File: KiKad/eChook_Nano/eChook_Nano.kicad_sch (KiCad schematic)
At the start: 52 parts, among them J1 Expansion, Q1 BC547, U1 Arduino_Nano_v3.x, U2 TSR_1-2450, U3 MCP6002-xP

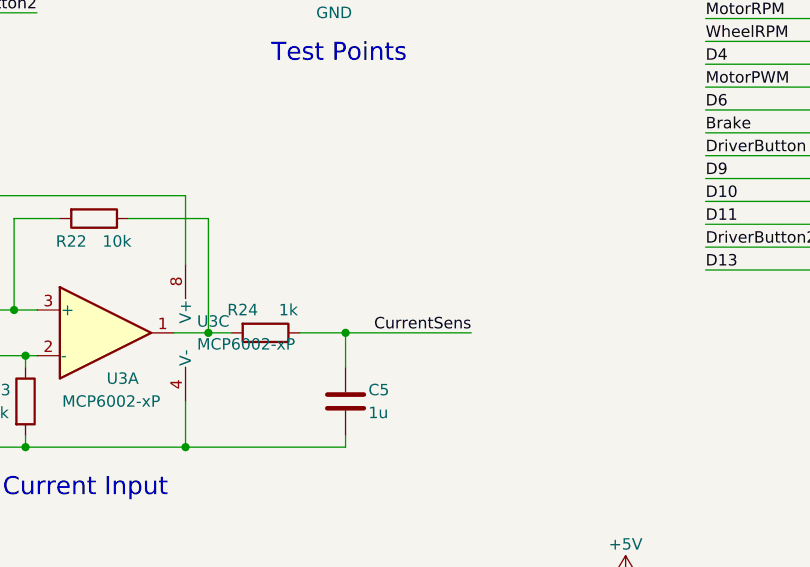
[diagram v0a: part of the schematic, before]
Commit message: Added 3D models and layout/silkscreen improvements
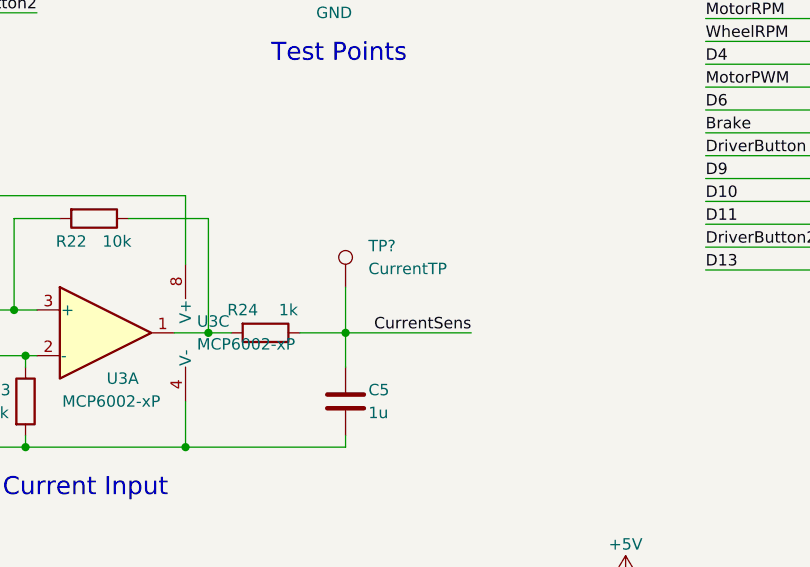
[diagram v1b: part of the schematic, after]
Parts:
- added TP?: CurrentTP, TestPoint:TestPoint_Pad_D3.0mm, symbol Connector:TestPoint
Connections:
- net CurrentSens: now also TP?.1
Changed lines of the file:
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@@
+    (stroke (width 0) (type default) (color 0 0 0 0))
+  )
+  (wire (pts (xy 93.98 124.46) (xy 93.98 129.54))
     (stroke (width 0) (type default) (color 0 0 0 0))
   )
@@
     )
     (property "Datasheet" "" (id 3) (at 34.29 187.325 0)
+      (effects (font (size 1.27 1.27)) hide)
+    )
+    (pin "1")
+  )
+  (symbol (lib_id "Connector:TestPoint") (at 93.98 124.46 0) (unit 1)
+    (in_bom yes) (on_board yes) (fields_autoplaced)
+    (property "Reference" "TP?" (id 0) (at 96.52 119.8879 0)
+      (effects (font (size 1.27 1.27)) (justify left))
+    )
+    (property "Value" "CurrentTP" (id 1) (at 96.52 122.4279 0)
+      (effects (font (size 1.27 1.27)) (justify left))
+    )
+    (property "Footprint" "TestPoint:TestPoint_Pad_D3.0mm" (id 2) (at 99.06 124.46 0)
+      (effects (font (size 1.27 1.27)) hide)
+    )
+    (property "Datasheet" "~" (id 3) (at 99.06 124.46 0)
       (effects (font (size 1.27 1.27)) hide)
     )
@@
       (reference "TP8") (unit 1) (value "ThrottleTP") (footprint "TestPoint:TestPoint_Pad_D3.0mm")
     )
+    (path "/dca3b52c-6cfb-46fe-8a89-560fb218906c"
+      (reference "TP?") (unit 1) (value "CurrentTP") (footprint "TestPoint:TestPoint_Pad_D3.0mm")
+    )
     (path "/ea7c53f9-3aa8-4198-9879-de95a5257915"

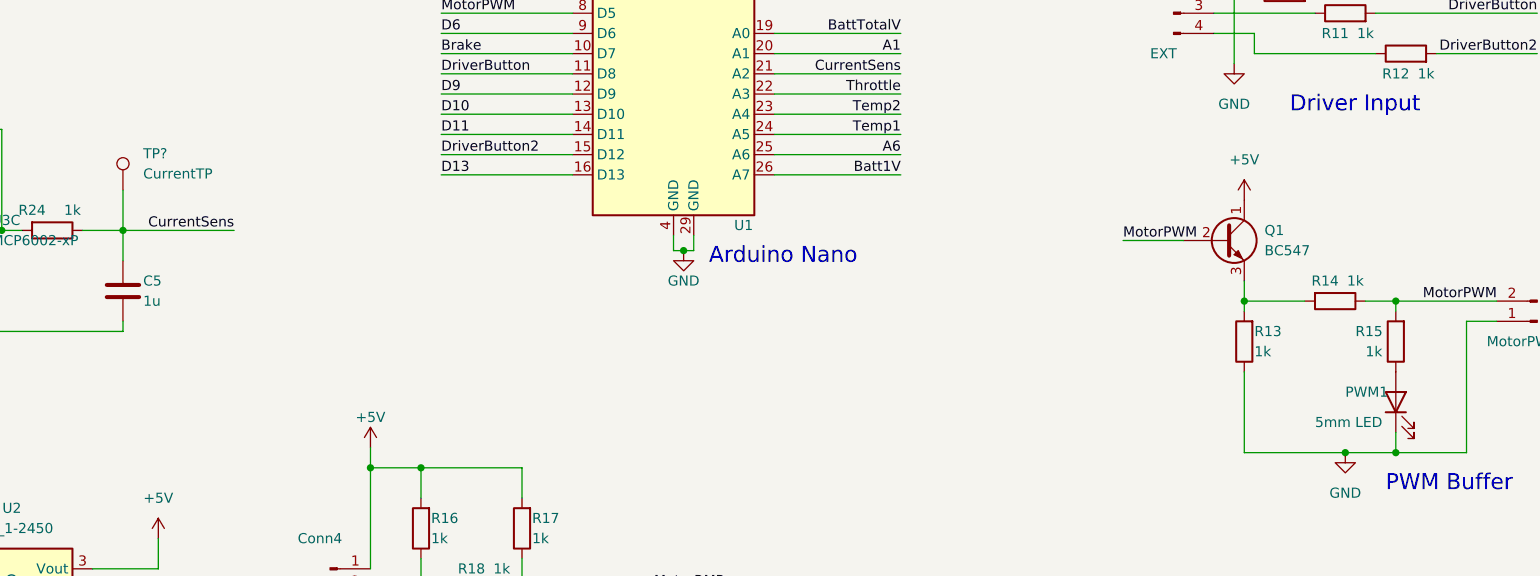
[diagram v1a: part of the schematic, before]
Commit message: Updated ext. pin out
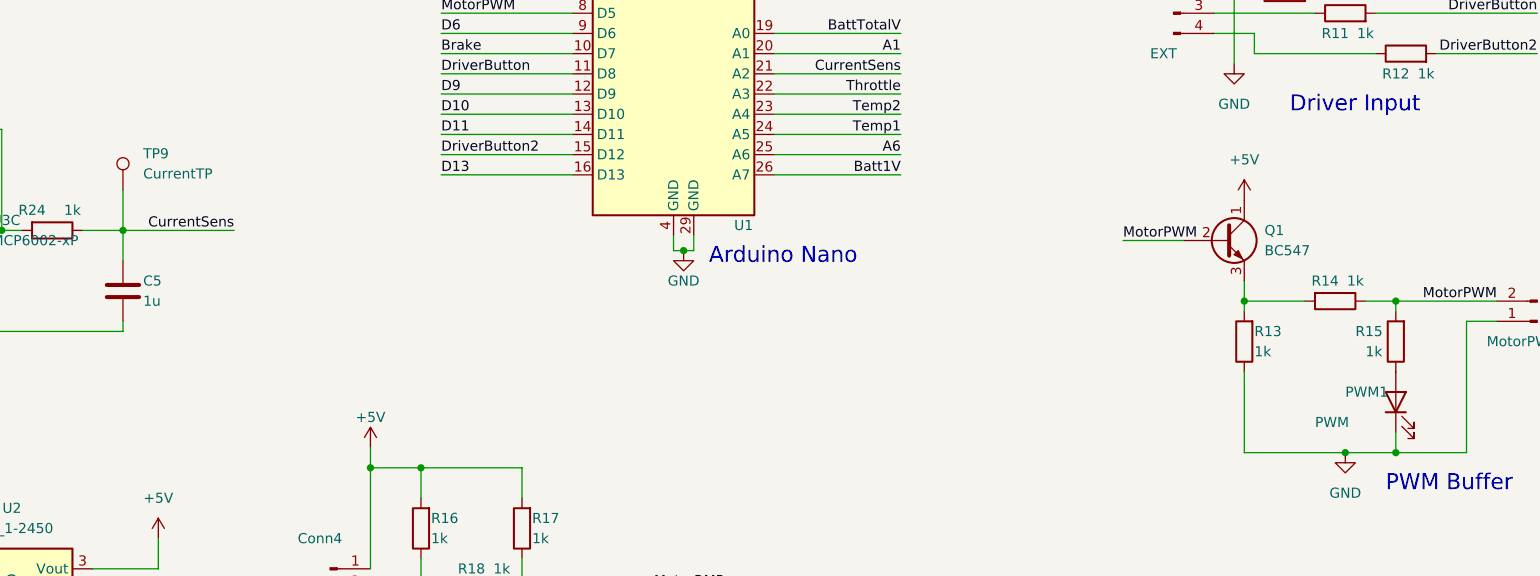
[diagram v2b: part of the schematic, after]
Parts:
- removed TP?: CurrentTP, TestPoint:TestPoint_Pad_D3.0mm, symbol Connector:TestPoint
- added TP9: CurrentTP, TestPoint:TestPoint_Pad_D3.0mm, symbol Connector:TestPoint
- PWM1: value 5mm LED -> PWM
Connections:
- net CurrentSens: now also TP9.1
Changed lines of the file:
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@@
       (effects (font (size 1.27 1.27)) (justify right))
     )
-    (property "Value" "5mm LED" (id 1) (at 243.84 153.67 90)
+    (property "Value" "PWM" (id 1) (at 243.84 153.67 90)
       (effects (font (size 1.27 1.27)) (justify right))
     )
@@
     (pin "3")
     (pin "4")
+  )
+  (symbol (lib_id "Connector:TestPoint") (at 93.98 124.46 0) (unit 1)
+    (in_bom yes) (on_board yes) (fields_autoplaced)
+    (property "Reference" "TP9" (id 0) (at 96.52 119.8879 0)
+      (effects (font (size 1.27 1.27)) (justify left))
+    )
+    (property "Value" "CurrentTP" (id 1) (at 96.52 122.4279 0)
+      (effects (font (size 1.27 1.27)) (justify left))
+    )
+    (property "Footprint" "TestPoint:TestPoint_Pad_D3.0mm" (id 2) (at 99.06 124.46 0)
+      (effects (font (size 1.27 1.27)) hide)
+    )
+    (property "Datasheet" "~" (id 3) (at 99.06 124.46 0)
+      (effects (font (size 1.27 1.27)) hide)
+    )
+    (pin "1")
   )
   (symbol (lib_id "Device:Polyfuse") (at 39.37 172.085 90) (unit 1)
@@
     )
     (property "Datasheet" "" (id 3) (at 34.29 187.325 0)
-      (effects (font (size 1.27 1.27)) hide)
-    )
-    (pin "1")
-  )
-  (symbol (lib_id "Connector:TestPoint") (at 93.98 124.46 0) (unit 1)
-    (in_bom yes) (on_board yes) (fields_autoplaced)
-    (property "Reference" "TP?" (id 0) (at 96.52 119.8879 0)
-      (effects (font (size 1.27 1.27)) (justify left))
-    )
-    (property "Value" "CurrentTP" (id 1) (at 96.52 122.4279 0)
-      (effects (font (size 1.27 1.27)) (justify left))
-    )
-    (property "Footprint" "TestPoint:TestPoint_Pad_D3.0mm" (id 2) (at 99.06 124.46 0)
-      (effects (font (size 1.27 1.27)) hide)
-    )
-    (property "Datasheet" "~" (id 3) (at 99.06 124.46 0)
       (effects (font (size 1.27 1.27)) hide)
     )
@@
     )
     (path "/480e869c-5ccd-450b-826a-11fb4eb4f7b7"
-      (reference "PWM1") (unit 1) (value "5mm LED") (footprint "LED_THT:LED_D5.0mm")
+      (reference "PWM1") (unit 1) (value "PWM") (footprint "LED_THT:LED_D5.0mm")
     )
     (path "/3dc302f0-822d-4e06-b3f8-7f67988ffc5d"
@@
       (reference "TP8") (unit 1) (value "ThrottleTP") (footprint "TestPoint:TestPoint_Pad_D3.0mm")
     )
-    (path "/dca3b52c-6cfb-46fe-8a89-560fb218906c"
-      (reference "TP?") (unit 1) (value "CurrentTP") (footprint "TestPoint:TestPoint_Pad_D3.0mm")
+    (path "/ae34ca85-3607-4b02-a720-7f76e8d7e328"
+      (reference "TP9") (unit 1) (value "CurrentTP") (footprint "TestPoint:TestPoint_Pad_D3.0mm")
     )
     (path "/ea7c53f9-3aa8-4198-9879-de95a5257915"

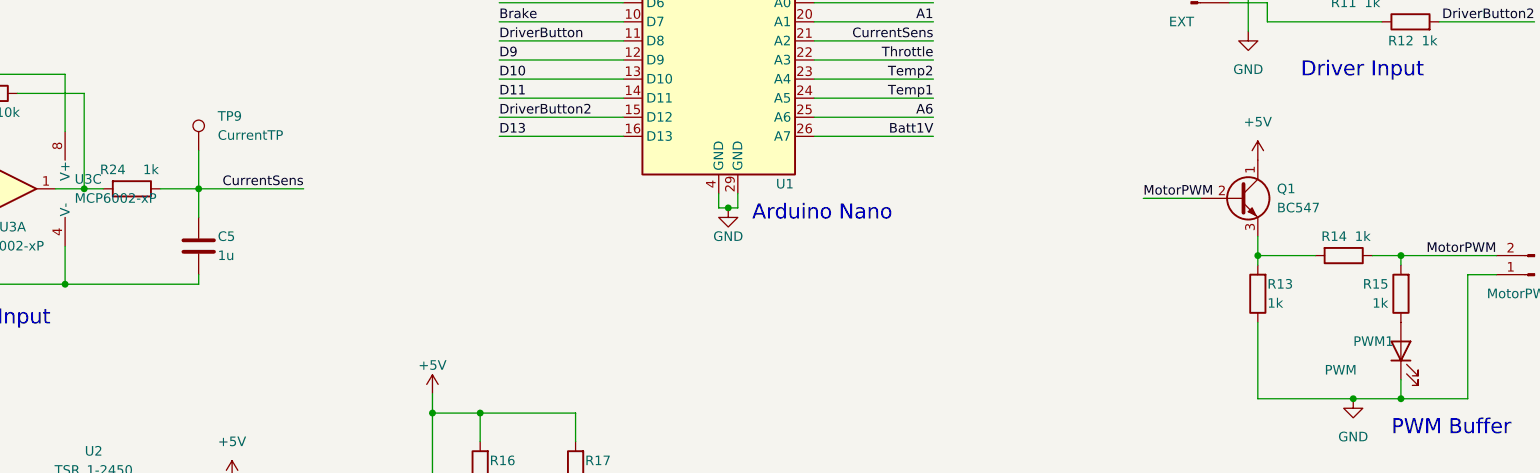
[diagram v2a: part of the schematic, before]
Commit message: R15 and R24 Value Correction, new IBOM
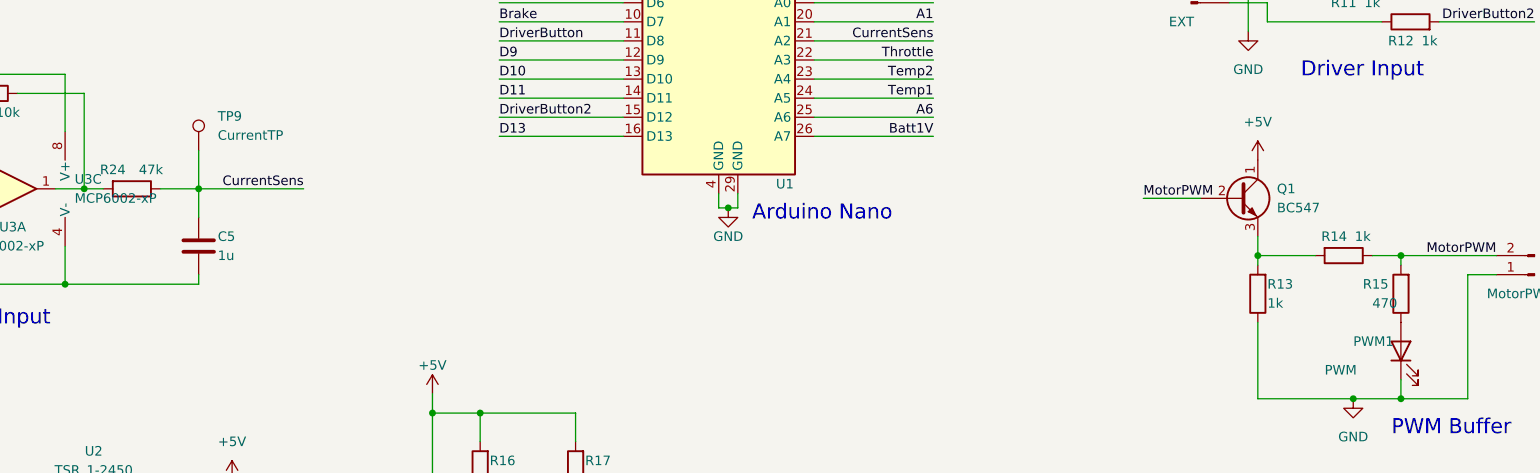
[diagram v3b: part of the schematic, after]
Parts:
- R15: value 1k -> 470
- R24: value 1k -> 47k
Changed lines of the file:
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@@
     (in_bom yes) (on_board yes)
     (property "Reference" "R24" (id 0) (at 82.55 127 90))
-    (property "Value" "1k" (id 1) (at 87.63 127 90))
+    (property "Value" "47k" (id 1) (at 87.63 127 90))
     (property "Footprint" "Resistor_THT:R_Axial_DIN0207_L6.3mm_D2.5mm_P10.16mm_Horizontal" (id 2) (at 85.09 127.762 90)
       (effects (font (size 1.27 1.27)) hide)
@@
       (effects (font (size 1.27 1.27)) (justify right))
     )
-    (property "Value" "1k" (id 1) (at 250.19 144.78 0)
+    (property "Value" "470" (id 1) (at 250.19 144.78 0)
       (effects (font (size 1.27 1.27)) (justify right))
     )
@@
     )
     (path "/b61d5fba-12dd-446b-9b20-46df956aea47"
-      (reference "R15") (unit 1) (value "1k") (footprint "Resistor_THT:R_Axial_DIN0207_L6.3mm_D2.5mm_P10.16mm_Horizontal")
+      (reference "R15") (unit 1) (value "470") (footprint "Resistor_THT:R_Axial_DIN0207_L6.3mm_D2.5mm_P10.16mm_Horizontal")
     )
     (path "/25b72dda-a4e7-4528-915a-a60a40acc81d"
@@
     )
     (path "/0621708e-181f-48fb-8cb9-d7919271dfca"
-      (reference "R24") (unit 1) (value "1k") (footprint "Resistor_THT:R_Axial_DIN0207_L6.3mm_D2.5mm_P10.16mm_Horizontal")
+      (reference "R24") (unit 1) (value "47k") (footprint "Resistor_THT:R_Axial_DIN0207_L6.3mm_D2.5mm_P10.16mm_Horizontal")
     )
     (path "/208ec1ff-0813-487b-bc7b-93951f623775"

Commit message: SMD Conversion
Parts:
- removed C1: C_Polarized, Capacitor_THT:CP_Radial_D5.0mm_P2.00mm, symbol Device:C_Polarized
- removed D1: DIODE, Diode_THT:D_DO-41_SOD81_P7.62mm_Horizontal, symbol Simulation_SPICE:DIODE
- removed PWM1: PWM, LED_THT:LED_D5.0mm, symbol Device:LED
- removed Q1: BC547, Package_TO_SOT_THT:TO-92L_Inline, symbol Device:Q_NPN_CBE
- added C1: 22u 10V, Capacitor_SMD:C_0805_2012Metric, symbol Device:C
- added C2: 47uf 63V, Capacitor_SMD:CP_Elec_10x10, symbol Device:C_Polarized
- added D1, D2, D4, D5, D6: SBD, Diode_SMD:D_SOD-523, symbol Device:D_Schottky
- added D3: LED, LED_SMD:LED_0603_1608Metric, symbol Device:LED
- added DZ1: 33v 35v 37v, Diode_SMD:D_SMB, symbol PCM_Diode_Zener_AKL:D_Zener_Generic
- added F1: Polyfuse, Fuse:Fuse_1206_3216Metric, symbol Device:Polyfuse
- added FS2: Polyfuse 300mA, Fuse:Fuse_0603_1608Metric, symbol Device:Polyfuse
- added LED1: LED_GREEN, LED_SMD:LED_0805_2012Metric, symbol Device:LED
- added Q2, Q3: Q_NMOS-D_Generic_GSD, PCM_Package_TO_SOT_SMD_AKL:SOT-23, symbol PCM_Transistor_MOSFET_AKL:Q_NMOS-D_Generic_GSD
- added R25, R26: 10k, Resistor_SMD:R_0805_2012Metric, symbol Device:R
- added R27: 3.3k 0.1%, Resistor_SMD:R_0603_1608Metric, symbol Device:R
- C3, C4, C5: footprint Capacitor_THT:C_Disc_D5.1mm_W3.2mm_P5.00mm -> Capacitor_SMD:C_0805_2012Metric
- FS1: value Polyfuse -> Polyfuse 300mA; footprint Capacitor_THT:C_Disc_D5.1mm_W3.2mm_P5.00mm -> Fuse:Fuse_0603_1608Metric; LCSC (none) -> C18377604
- R1, R10, R11, R12, R14, R18, R19, R2, R20, R21, R22, R23, R3, R4, R5, R6, R7, R8, R9: footprint Resistor_THT:R_Axial_DIN0207_L6.3mm_D2.5mm_P10.16mm_Horizontal -> Resistor_SMD:R_0805_2012Metric
- R13, R16, R17: value 1k -> 10k; footprint Resistor_THT:R_Axial_DIN0207_L6.3mm_D2.5mm_P10.16mm_Horizontal -> Resistor_SMD:R_0805_2012Metric
- R15: value 470 -> 10k; footprint Resistor_THT:R_Axial_DIN0207_L6.3mm_D2.5mm_P10.16mm_Horizontal -> Resistor_SMD:R_0805_2012Metric
- R24: value 47k -> 10k; footprint Resistor_THT:R_Axial_DIN0207_L6.3mm_D2.5mm_P10.16mm_Horizontal -> Resistor_SMD:R_0805_2012Metric
- TP1, TP2, TP3, TP4, TP5, TP6, TP7, TP8, TP9, U1: now not fitted
- U2: LCSC (none) -> C5369649
- U3: footprint Package_DIP:DIP-8_W7.62mm_LongPads -> Package_SO:SOIC-8_3.9x4.9mm_P1.27mm; LCSC (none) -> C7377
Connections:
- net MotorRMP is gone; now on net MotorRPM: R18.1
- net +12V: now also FS2.2; no longer Conn2.2 (Pin_2)
- net +24V: now also C2.1, DZ1.1 (K)
- net +5V: now also C1.1, D1.1 (K), D2.1 (K), D4.1 (K), D5.1 (K), D6.1 (K), F1.1, R25.2, R26.1, R27.2
- net Batt1v: now also D5.2 (A)
- net BattTotalV: now also D4.2 (A)
- net GND: now also R13.2, R23.1, C1.2, C2.2, DZ1.2 (A), LED1.1 (K), Q2.2 (S), Q3.2 (S); no longer R13.1, R23.2
- net MotorPWM: now also R13.1, Q2.1 (G); no longer Conn8.2 (Pin_2), R14.1, R15.2
- net Temp1: now also D2.2 (A)
- net Temp2: now also D1.2 (A)
- net Throttle: now also D6.2 (A)
- net at R14.2: now also Q3.3 (D), R25.1; no longer R13.2
- net at R20.1, U3.2 (-): now also R23.2; no longer R23.1
- net at R15.1: now also LED1.2 (A)
- new net: Q2.3 (D), Q3.1 (G), R26.2
- new net: Conn8.2 (Pin_2), R14.1, R15.2
- new net: Conn2.2 (Pin_2), FS2.1
- new net: D3.2 (A), R27.1
- new net 5V_Fused: D3.1 (K), F1.2
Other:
- note added: "Overcurrent LED"
- moved on the sheet: Conn2, Conn4, Conn8, FS1, R14, R16, R17, R18, R19, U2

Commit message: Routing Complete
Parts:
- removed F1: Polyfuse, Fuse:Fuse_1206_3216Metric, symbol Device:Polyfuse
- added D10, D11, D7, D8, D9: LED, LED_SMD:LED_0603_1608Metric, symbol Device:LED
- added FS3, FS4, FS5, FS6, FS7: Polyfuse 300mA, Fuse:Fuse_0603_1608Metric, symbol Device:Polyfuse
- added R28: 10k, Resistor_SMD:R_0805_2012Metric, symbol Device:R
- added R29, R30, R31, R32: 1k, Resistor_SMD:R_0805_2012Metric, symbol Device:R
- C1: LCSC (none) -> C45783
- C3, C4, C5: LCSC (none) -> C28323
- Conn1, Conn4, Conn5: LCSC (none) -> C441206
- Conn2: LCSC (none) -> C8406
- Conn3, Conn6: LCSC (none) -> C441205
- Conn7: LCSC (none) -> C5224026
- Conn8: LCSC (none) -> C441204
- D3: LCSC C72041 -> C2286
- J1: LCSC (none) -> C2685212
- R1, R3: LCSC (none) -> C17840
- R10, R11, R12, R14, R18, R19, R6, R8, R9: LCSC (none) -> C17513
- R13, R15, R16, R17, R22, R23, R24, R25, R26, R5, R7: LCSC (none) -> C17414
- R2, R4: LCSC (none) -> C17490
- R20, R21: LCSC (none) -> C17673
- R27: value 3.3k 0.1% -> 1k; footprint Resistor_SMD:R_0603_1608Metric -> Resistor_SMD:R_0805_2012Metric; LCSC C2686444 -> C17513; MPN ARG03BTC3301 -> (none); Manufacturer Viking Tech -> (none)
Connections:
- net Batt1V is gone; now on net Batt1v: U1.26 (A7)
- net +24V: now also D7.1 (K)
- net +5V: now also FS3.2, FS4.2, FS5.2, FS6.2, FS7.2, R29.2, R30.2, R31.2, R32.2; no longer Conn1.1 (Pin_1), Conn4.1 (Pin_1), Conn6.1 (Pin_1), Conn7.2 (Pin_2), J1.1 (Pin_1)
- net 24vIn: now reaches Conn2.1 (Pin_1), FS1.1
- net 24vIn: now also R28.1
- net 5V_Fused: no longer names the net of D3.1 (K)
- net 5V_Fused: now also Conn6.1 (Pin_1), FS3.1
- new net: Conn4.1 (Pin_1), D11.1 (K), FS7.1
- new net: D11.2 (A), R32.1
- new net: D7.2 (A), R28.2
- new net: D9.2 (A), R30.1
- new net: Conn7.2 (Pin_2), D8.1 (K), FS4.1
- new net: Conn1.1 (Pin_1), D10.1 (K), FS6.1
- new net: D8.2 (A), R29.1
- new net: D10.2 (A), R31.1
- new net: D9.1 (K), FS5.1, J1.1 (Pin_1)
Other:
- moved on the sheet: C5, Conn1, Conn6, Conn7, D3, D6, R16, R17, R18, R19, R20, R21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

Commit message: production ready
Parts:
- removed TP4: GNDTP, TestPoint:TestPoint_Pad_D3.0mm, symbol Connector:TestPoint
- added JP1, JP2: SolderJumper_3_Bridged12, Jumper:SolderJumper-3_P1.3mm_Bridged12_RoundedPad1.0x1.5mm, symbol Jumper:SolderJumper_3_Bridged12
- added JP3: SolderJumper_2_Open, Jumper:SolderJumper-2_P1.3mm_Open_RoundedPad1.0x1.5mm, symbol Jumper:SolderJumper_2_Open
- added R33: 1k, Resistor_SMD:R_0805_2012Metric, symbol Device:R
- added R34: 10k, Resistor_SMD:R_0805_2012Metric, symbol Device:R
- FS1, FS2, FS3, FS4, FS5, FS6, FS7: MPN (none) -> BHFUSE BSMD0603-010-36V
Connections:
- net +5V: now also R15.2
- net A1: now also J1.10 (Pin_10), JP1.3 (B); no longer J1.11 (Pin_11)
- net A6: now also J1.13 (Pin_13), JP2.3 (B); no longer J1.12 (Pin_12)
- net D4: now also JP3.1 (A)
- net D6: now also J1.9 (Pin_9); no longer J1.10 (Pin_10)
- net DriverButton: now also J1.8 (Pin_8); no longer J1.9 (Pin_9)
- net DriverButton2: no longer J1.8 (Pin_8)
- net EN: now also JP3.2 (B)
- net GND: now also R34.2; no longer J1.13 (Pin_13), LED1.1 (K)
- net MotorPWM: now also R33.2; no longer Q2.1 (G), R13.1
- net Temp1: now also JP1.2 (C); no longer U1.24 (A5)
- net Temp2: now also JP2.2 (C); no longer U1.23 (A4)
- net Throttle: now also R34.1
- net at Q2.3 (D), Q3.1 (G), R26.2: now also LED1.1 (K)
- net at Conn8.2 (Pin_2), R14.1: no longer R15.2
- new net: Q2.1 (G), R13.1, R33.1
- new net A4: J1.11 (Pin_11), JP2.1 (A), U1.23 (A4)
- new net A5: J1.12 (Pin_12), JP1.1 (A), U1.24 (A5)
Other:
- note added: "Jumpers"
- note removed: "Test Points"
- moved on the sheet: Conn8, LED1, Q2, Q3, R13, R14, R15, R25, R26, TP3, U1

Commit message: Fixing V2.0a issues
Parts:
- added D12: LED_GREEN, LED_SMD:LED_0805_2012Metric, symbol Device:LED
- added R35: 10k, Resistor_SMD:R_0805_2012Metric, symbol Device:R
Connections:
- net +24V: now also D12.2 (A)
- net 24vIn: now also R35.1
- net at R20.1, R23.2: now also U3.3 (+); no longer U3.2 (-)
- net at R21.1, R22.2: now also U3.2 (-); no longer U3.3 (+)
- new net: D12.1 (K), R35.2
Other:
- note added: "Battery Voltage Input Dividers"
- note added: "Power LED"
- note removed: "Voltage Dividers"
- moved on the sheet: C1, C2, C3, C4, C5, Conn1, Conn2, Conn3, Conn4, Conn5, Conn6, Conn7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
